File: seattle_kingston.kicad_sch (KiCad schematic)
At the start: 31 parts

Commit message: single ferry track checkpoint
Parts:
- removed LED470, LED471, LED472, LED473, LED474, LED475, LED476, LED477, LED478, LED479, LED480, LED481, LED485, LED486, LED487: WS2812B-2020, EasyEDA:LED-SMD_4P-L2.0-W2.0-TL_WS2812B-2020, symbol EasyEDA:WS2812B-2020
- added LED901, LED902, LED918: WS2812B-2020, EasyEDA:LED-SMD_4P-L2.0-W2.0-TL_WS2812B-2020, symbol EasyEDA:WS2812B-2020
- renumbered LED435 to LED903, LED436 to LED904, LED437 to LED905, LED438 to LED906, LED439 to LED907, LED440 to LED908, LED441 to LED909, LED442 to LED910, LED443 to LED911, LED444 to LED912, LED445 to LED913, LED446 to LED914, LED482 to LED915, LED483 to LED916, LED484 to LED917
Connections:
- net +VLED: now also LED903.4 (VDD), LED901.4 (VDD), LED902.4 (VDD), LED918.4 (VDD)
- net GND: now also LED901.2 (GND), LED901.3 (DI), LED902.2 (GND), LED918.2 (GND); no longer LED903.3 (DI)
- net at LED917.1 (DO): now also LED918.3 (DI); no longer LED434.4 (DIN)
- new net: LED902.1 (DO), LED903.3 (DI)
- new net: LED901.1 (DO), LED902.3 (DI)
- new net: LED434.4 (DIN), LED918.1 (DO)
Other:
- moved on the sheet: LED434, LED903, LED904, LED905, LED906, LED907, LED908, LED909, LED910, LED911, LED912, LED913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

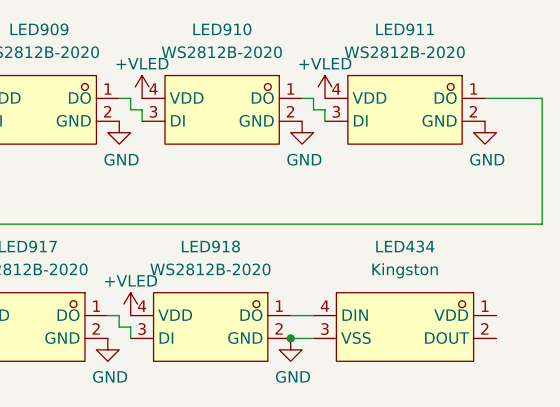
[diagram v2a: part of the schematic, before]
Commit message: Add rail labels
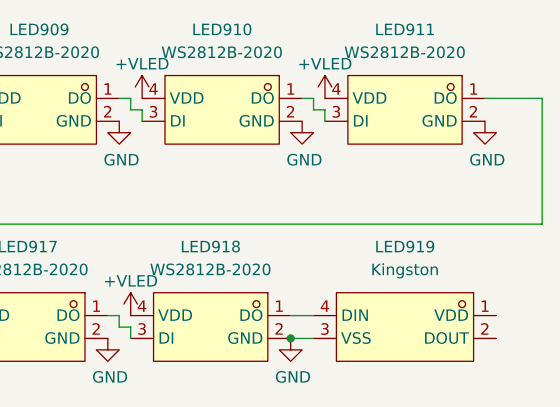
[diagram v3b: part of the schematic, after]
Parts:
- renumbered LED434 to LED919
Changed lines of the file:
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@@
 		(in_pos_files yes)
 		(dnp no)
-		(property "Reference" "LED434"
+		(property "Reference" "LED919"
 			(at 238.76 49.53 0)
 			(show_name no)
@@
 			(project "transit"
 				(path "/3763eade-a8c8-4ec0-9cf2-9db4442b4ee5/153adc6e-a3b0-4527-a19a-87e28aab4b4d/d3b1612b-935b-4481-9997-ae3b3118dbce"
-					(reference "LED434")
+					(reference "LED919")
 					(unit 1)
 				)

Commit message: junction checkpoint
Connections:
- net GND: no longer LED901.3 (DI)
- new net BAINBRIDGE_X_KINGSTON: LED901.3 (DI)
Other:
- moved on the sheet: LED901, LED902, LED903, LED904, LED905, LED906, LED907, LED908, LED909, LED910, LED911, LED912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

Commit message: routing complete
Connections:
- net +VLED: now also LED919.1 (VDD)
- net KINGSTON_EDMONDS: now reaches LED919.2 (DOUT)
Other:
- moved on the sheet: LED901, LED902, LED903, LED904, LED905, LED906, LED907, LED908, LED909, LED910, LED911, LED912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

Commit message: rev-b validation run
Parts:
- LED901, LED902, LED903, LED904, LED905, LED906, LED907, LED908, LED909, LED910, LED911, LED912, LED913, LED914, LED915, LED916, LED917, LED918: LCSC Part C965555 -> C52917434
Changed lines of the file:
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@@
 			)
 		)
-		(property "Datasheet" "https://lcsc.com/product-detail/Light-Emitting-Diodes-LED_Worldsemi-WS2812B-2020_C965555.html"
+		(property "Datasheet" "https://lcsc.com/product-detail/Light-Emitting-Diodes-LED_Worldsemi-WS2812B-2020_C52917434.html"
 			(at 62.23 45.72 0)
 			(hide yes)
@@
 			)
 		)
-		(property "LCSC Part" "C965555"
+		(property "LCSC Part" "C52917434"
 			(at 62.23 48.26 0)
 			(hide yes)
@@
 			)
 		)
-		(property "Datasheet" "https://lcsc.com/product-detail/Light-Emitting-Diodes-LED_Worldsemi-WS2812B-2020_C965555.html"
+		(property "Datasheet" "https://lcsc.com/product-detail/Light-Emitting-Diodes-LED_Worldsemi-WS2812B-2020_C52917434.html"
 			(at 205.74 69.85 0)
 			(hide yes)
@@
 			)
 		)
-		(property "LCSC Part" "C965555"
+		(property "LCSC Part" "C52917434"
 			(at 205.74 72.39 0)
 			(hide yes)
@@
 			)
 		)
-		(property "Datasheet" "https://lcsc.com/product-detail/Light-Emitting-Diodes-LED_Worldsemi-WS2812B-2020_C965555.html"
+		(property "Datasheet" "https://lcsc.com/product-detail/Light-Emitting-Diodes-LED_Worldsemi-WS2812B-2020_C52917434.html"
 			(at 165.1 69.85 0)
 			(hide yes)
@@
 			)
 		)
-		(property "LCSC Part" "C965555"
+		(property "LCSC Part" "C52917434"
 			(at 165.1 72.39 0)
 			(hide yes)
@@
 			)
 		)
-		(property "Datasheet" "https://lcsc.com/product-detail/Light-Emitting-Diodes-LED_Worldsemi-WS2812B-2020_C965555.html"
+		(property "Datasheet" "https://lcsc.com/product-detail/Light-Emitting-Diodes-LED_Worldsemi-WS2812B-2020_C52917434.html"
 			(at 185.42 69.85 0)
 			(hide yes)
@@
 			)
 		)
-		(property "LCSC Part" "C965555"
+		(property "LCSC Part" "C52917434"
 			(at 185.42 72.39 0)
 			(hide yes)
@@
 			)
 		)
-		(property "Datasheet" "https://lcsc.com/product-detail/Light-Emitting-Diodes-LED_Worldsemi-WS2812B-2020_C965555.html"
+		(property "Datasheet" "https://lcsc.com/product-detail/Light-Emitting-Diodes-LED_Worldsemi-WS2812B-2020_C52917434.html"
 			(at 101.6 69.85 0)
 			(hide yes)
@@
 			)
 		)
-		(property "LCSC Part" "C965555"
+		(property "LCSC Part" "C52917434"
 			(at 101.6 72.39 0)
 			(hide yes)
@@
 			)
 		)
-		(property "Datasheet" "https://lcsc.com/product-detail/Light-Emitting-Diodes-LED_Worldsemi-WS2812B-2020_C965555.html"
+		(property "Datasheet" "https://lcsc.com/product-detail/Light-Emitting-Diodes-LED_Worldsemi-WS2812B-2020_C52917434.html"
 			(at 186.69 45.72 0)
 			(hide yes)
@@
 			)
 		)
-		(property "LCSC Part" "C965555"
+		(property "LCSC Part" "C52917434"
 			(at 186.69 48.26 0)
 			(hide yes)
@@
 			)
 		)
-		(property "Datasheet" "https://lcsc.com/product-detail/Light-Emitting-Diodes-LED_Worldsemi-WS2812B-2020_C965555.html"
+		(property "Datasheet" "https://lcsc.com/product-detail/Light-Emitting-Diodes-LED_Worldsemi-WS2812B-2020_C52917434.html"
 			(at 227.33 45.72 0)
 			(hide yes)
@@
 			)
 		)
-		(property "LCSC Part" "C965555"
+		(property "LCSC Part" "C52917434"
 			(at 227.33 48.26 0)
 			(hide yes)
@@
 			)
 		)
-		(property "Datasheet" "https://lcsc.com/product-detail/Light-Emitting-Diodes-LED_Worldsemi-WS2812B-2020_C965555.html"
+		(property "Datasheet" "https://lcsc.com/product-detail/Light-Emitting-Diodes-LED_Worldsemi-WS2812B-2020_C52917434.html"
 			(at 86.36 45.72 0)
 			(hide yes)
@@
 			)
 		)
-		(property "LCSC Part" "C965555"
+		(property "LCSC Part" "C52917434"
 			(at 86.36 48.26 0)
 			(hide yes)
@@
 			)
 		)
-		(property "Datasheet" "https://lcsc.com/product-detail/Light-Emitting-Diodes-LED_Worldsemi-WS2812B-2020_C965555.html"
+		(property "Datasheet" "https://lcsc.com/product-detail/Light-Emitting-Diodes-LED_Worldsemi-WS2812B-2020_C52917434.html"
 			(at 226.06 69.85 0)
 			(hide yes)
@@
 			)
 		)
-		(property "LCSC Part" "C965555"
+		(property "LCSC Part" "C52917434"
 			(at 226.06 72.39 0)
 			(hide yes)
@@
 			)
 		)
-		(property "Datasheet" "https://lcsc.com/product-detail/Light-Emitting-Diodes-LED_Worldsemi-WS2812B-2020_C965555.html"
+		(property "Datasheet" "https://lcsc.com/product-detail/Light-Emitting-Diodes-LED_Worldsemi-WS2812B-2020_C52917434.html"
 			(at 41.91 45.72 0)
 			(hide yes)
@@
 			)
 		)
-		(property "LCSC Part" "C965555"
+		(property "LCSC Part" "C52917434"
 			(at 41.91 48.26 0)
 			(hide yes)
@@
 			)
 		)
-		(property "Datasheet" "https://lcsc.com/product-detail/Light-Emitting-Diodes-LED_Worldsemi-WS2812B-2020_C965555.html"
+		(property "Datasheet" "https://lcsc.com/product-detail/Light-Emitting-Diodes-LED_Worldsemi-WS2812B-2020_C52917434.html"
 			(at 121.92 69.85 0)
 			(hide yes)
@@
 			)
 		)
-		(property "LCSC Part" "C965555"
+		(property "LCSC Part" "C52917434"
 			(at 121.92 72.39 0)
 			(hide yes)
@@
 			)
 		)
-		(property "Datasheet" "https://lcsc.com/product-detail/Light-Emitting-Diodes-LED_Worldsemi-WS2812B-2020_C965555.html"
+		(property "Datasheet" "https://lcsc.com/product-detail/Light-Emitting-Diodes-LED_Worldsemi-WS2812B-2020_C52917434.html"
 			(at 142.24 69.85 0)
 			(hide yes)
@@
 			)
 		)
-		(property "LCSC Part" "C965555"
+		(property "LCSC Part" "C52917434"
 			(at 142.24 72.39 0)
 			(hide yes)
@@
 			)
 		)
-		(property "Datasheet" "https://lcsc.com/product-detail/Light-Emitting-Diodes-LED_Worldsemi-WS2812B-2020_C965555.html"
+		(property "Datasheet" "https://lcsc.com/product-detail/Light-Emitting-Diodes-LED_Worldsemi-WS2812B-2020_C52917434.html"
 			(at 247.65 45.72 0)
 			(hide yes)
@@
 			)
 		)
-		(property "LCSC Part" "C965555"
+		(property "LCSC Part" "C52917434"
 			(at 247.65 48.26 0)
 			(hide yes)
@@
 			)
 		)
-		(property "Datasheet" "https://lcsc.com/product-detail/Light-Emitting-Diodes-LED_Worldsemi-WS2812B-2020_C965555.html"
+		(property "Datasheet" "https://lcsc.com/product-detail/Light-Emitting-Diodes-LED_Worldsemi-WS2812B-2020_C52917434.html"
 			(at 106.68 45.72 0)
 			(hide yes)
@@
 			)
 		)
-		(property "LCSC Part" "C965555"
+		(property "LCSC Part" "C52917434"
 			(at 106.68 48.26 0)
 			(hide yes)
@@
 			)
 		)
-		(property "Datasheet" "https://lcsc.com/product-detail/Light-Emitting-Diodes-LED_Worldsemi-WS2812B-2020_C965555.html"
+		(property "Datasheet" "https://lcsc.com/product-detail/Light-Emitting-Diodes-LED_Worldsemi-WS2812B-2020_C52917434.html"
 			(at 125.73 45.72 0)
 			(hide yes)
@@
 			)
 		)
-		(property "LCSC Part" "C965555"
+		(property "LCSC Part" "C52917434"
 			(at 125.73 48.26 0)
 			(hide yes)
@@
 			)
 		)
-		(property "Datasheet" "https://lcsc.com/product-detail/Light-Emitting-Diodes-LED_Worldsemi-WS2812B-2020_C965555.html"
+		(property "Datasheet" "https://lcsc.com/product-detail/Light-Emitting-Diodes-LED_Worldsemi-WS2812B-2020_C52917434.html"
 			(at 166.37 45.72 0)
 			(hide yes)
@@
 			)
 		)
-		(property "LCSC Part" "C965555"
+		(property "LCSC Part" "C52917434"
 			(at 166.37 48.26 0)
 			(hide yes)
@@
 			)
 		)
-		(property "Datasheet" "https://lcsc.com/product-detail/Light-Emitting-Diodes-LED_Worldsemi-WS2812B-2020_C965555.html"
+		(property "Datasheet" "https://lcsc.com/product-detail/Light-Emitting-Diodes-LED_Worldsemi-WS2812B-2020_C52917434.html"
 			(at 207.01 45.72 0)
 			(hide yes)
@@
 			)
 		)
-		(property "LCSC Part" "C965555"
+		(property "LCSC Part" "C52917434"
 			(at 207.01 48.26 0)
 			(hide yes)
@@
 			)
 		)
-		(property "Datasheet" "https://lcsc.com/product-detail/Light-Emitting-Diodes-LED_Worldsemi-WS2812B-2020_C965555.html"
+		(property "Datasheet" "https://lcsc.com/product-detail/Light-Emitting-Diodes-LED_Worldsemi-WS2812B-2020_C52917434.html"
 			(at 146.05 45.72 0)
 			(hide yes)
@@
 			)
 		)
-		(property "LCSC Part" "C965555"
+		(property "LCSC Part" "C52917434"
 			(at 146.05 48.26 0)
 			(hide yes)
